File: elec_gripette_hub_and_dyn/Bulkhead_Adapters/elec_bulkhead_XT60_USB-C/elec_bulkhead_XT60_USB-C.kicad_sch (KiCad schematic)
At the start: 14 parts, among them J1 USB-C Rec. Vert., J2 JST EH 2, J3 XT60, J4 pico4

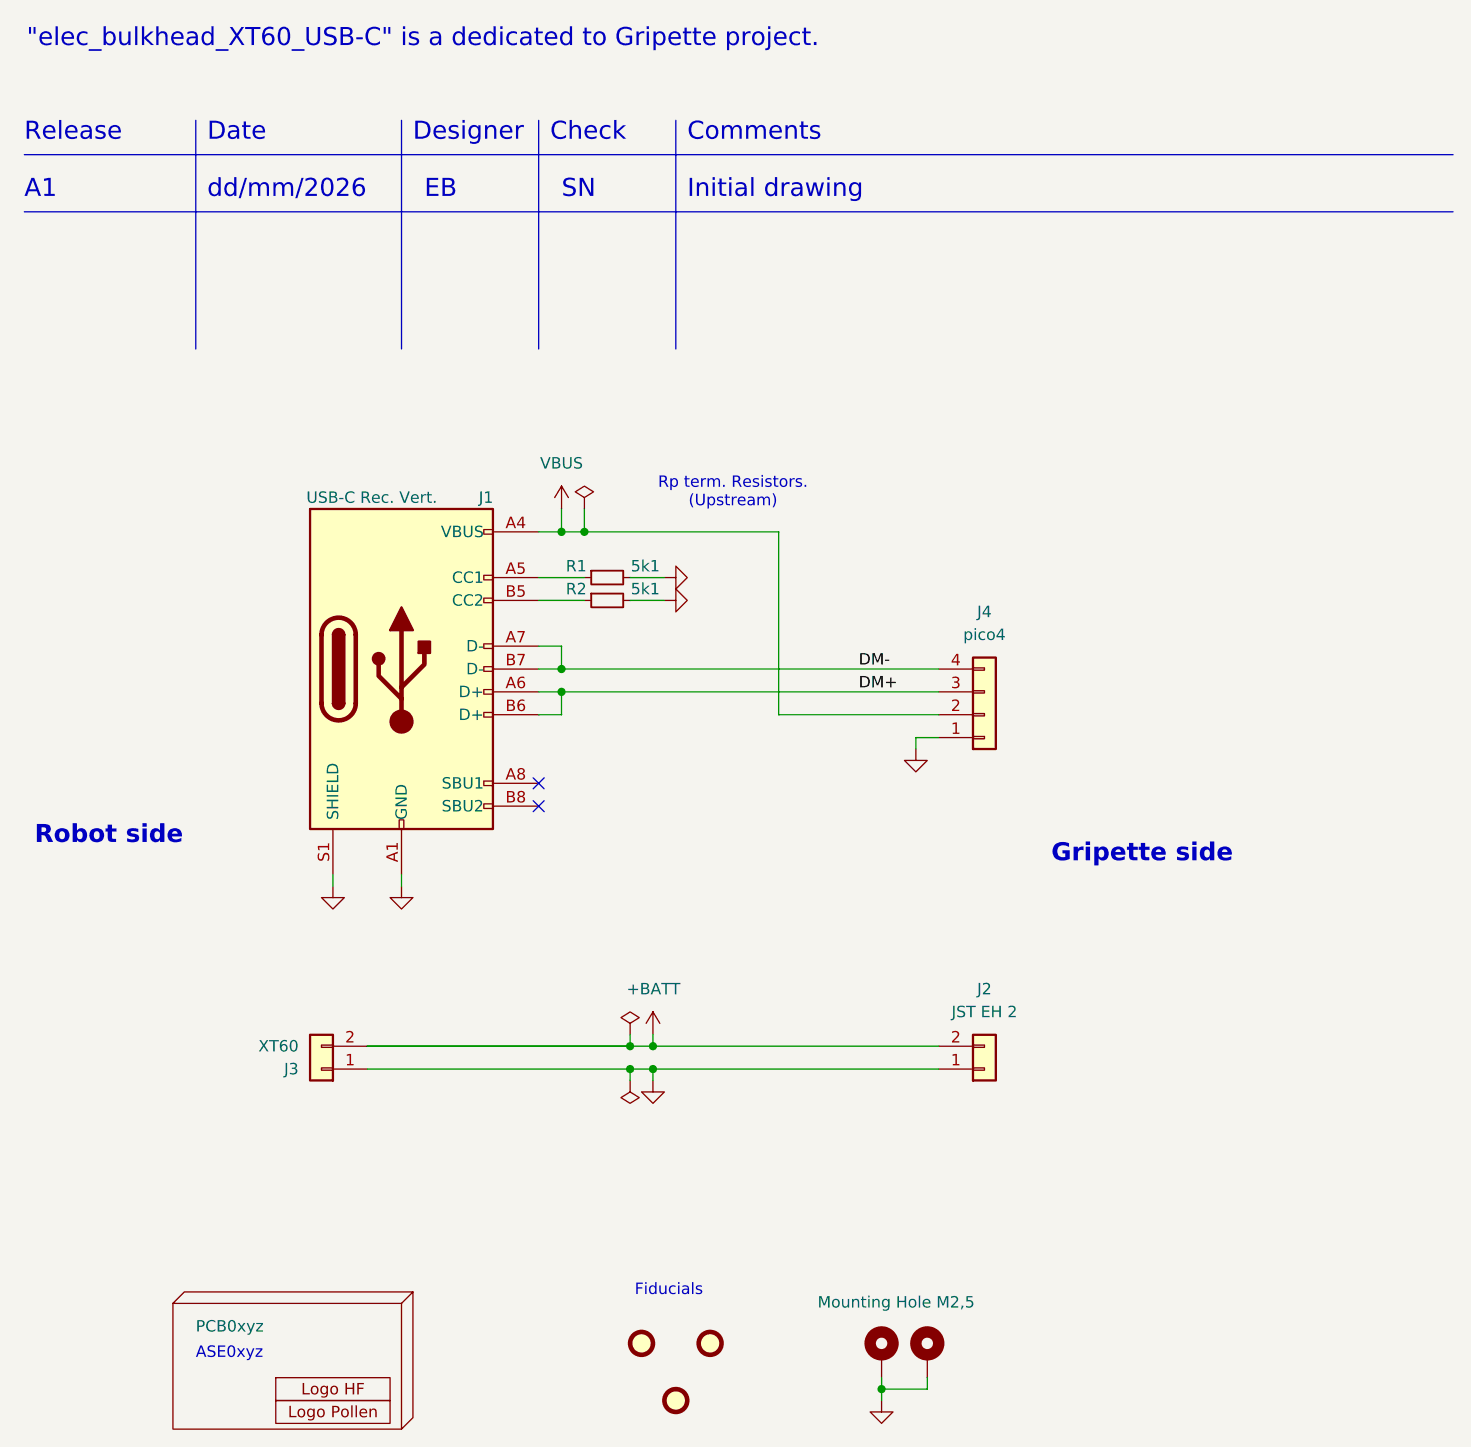
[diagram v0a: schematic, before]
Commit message: [update] Gripette bulkhead ready for production.
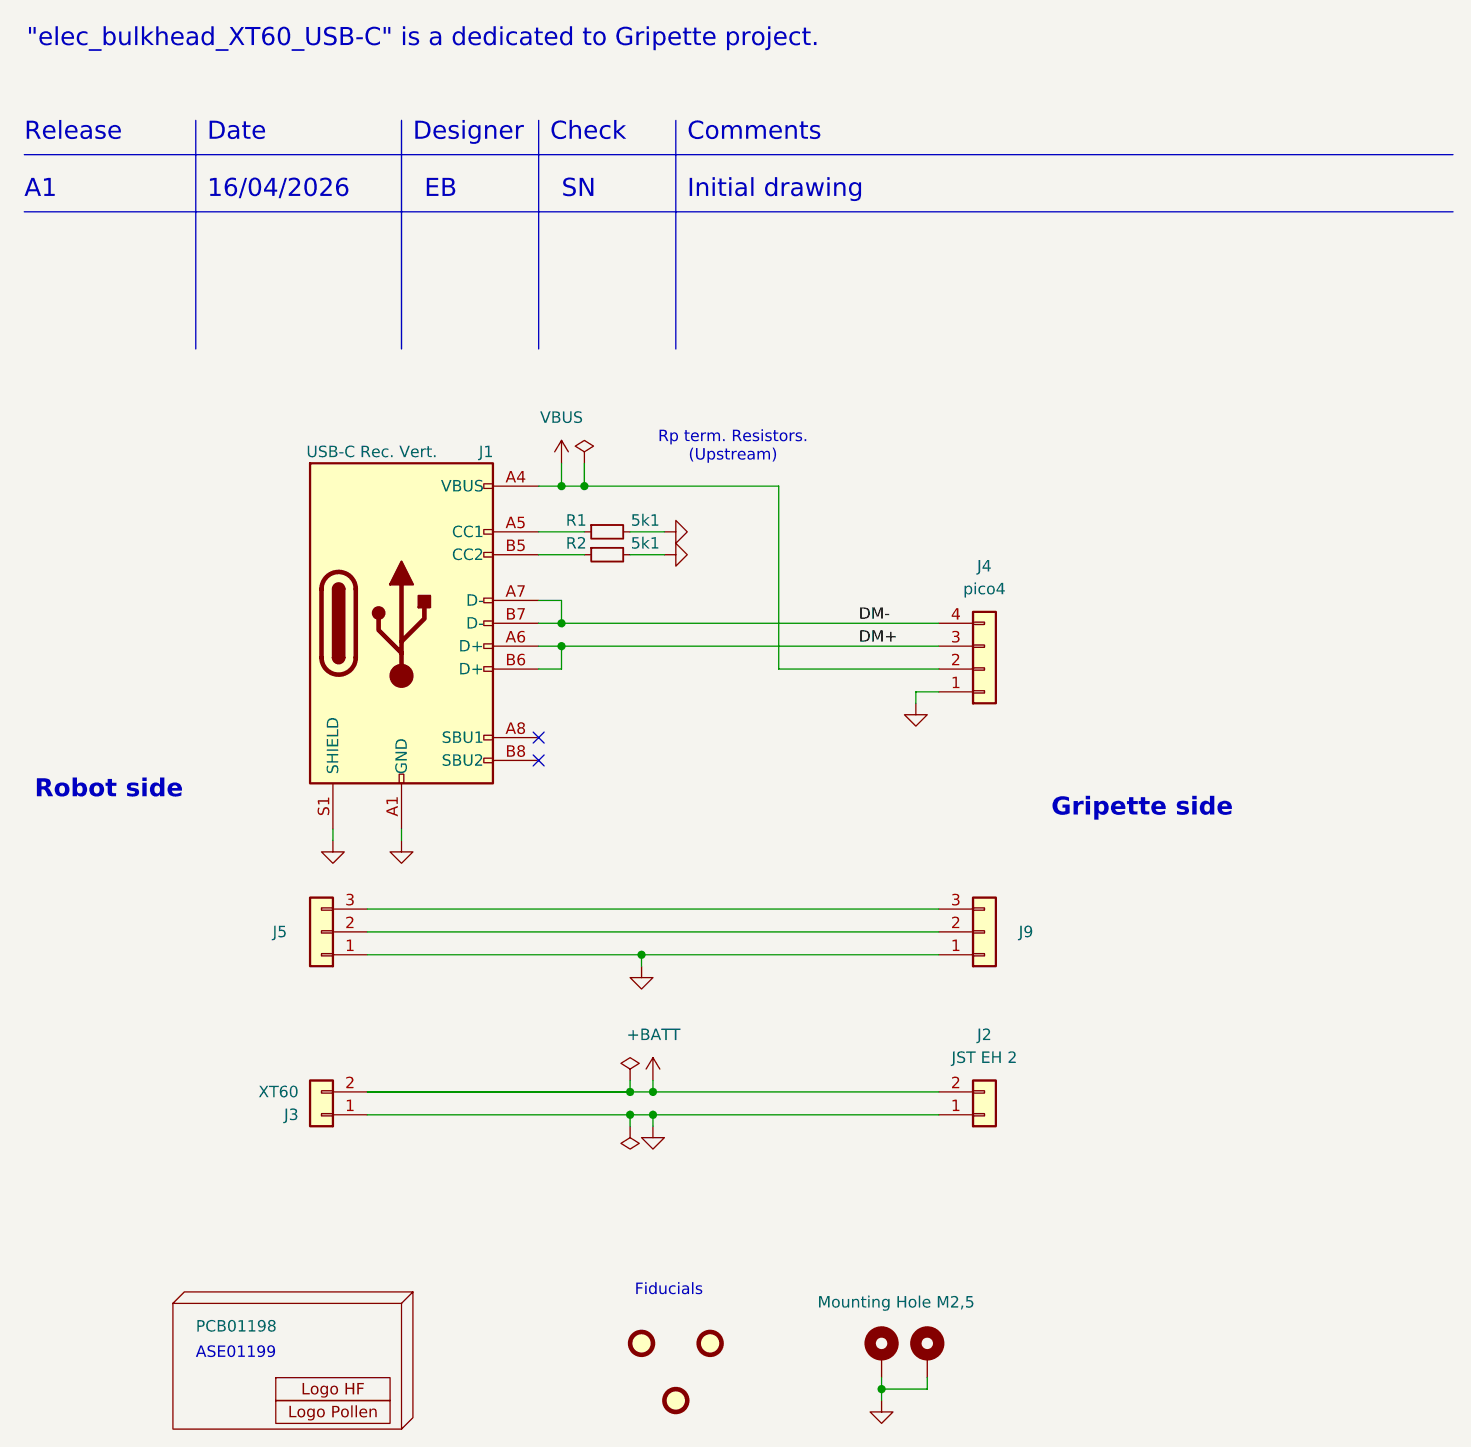
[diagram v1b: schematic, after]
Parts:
- added J5: Dynamixel-3, Connector_JST:JST_EH_B3B-EH-A_1x03_P2.50mm_Vertical, symbol Connector_Generic:Conn_01x03
- added J9: Dynamixel-3, Connector_JST:JST_EH_S3B-EH_1x03_P2.50mm_Horizontal, symbol Connector_Generic:Conn_01x03
- H1: value PCB0xyz -> PCB01198
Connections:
- net GND: now also J5.1 (Pin_1), J9.1 (Pin_1)
- new net: J5.2 (Pin_2), J9.2 (Pin_2)
- new net: J5.3 (Pin_3), J9.3 (Pin_3)
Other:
- note added: "16/04/2026"
- note added: "ASE01199"
- note removed: "ASE0xyz"
- note removed: "dd/mm/2026"
- moved on the sheet: J1, J2, J3, J4, R1, R2
